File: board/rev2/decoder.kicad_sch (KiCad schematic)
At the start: 2 parts, among them U9 74VHC161

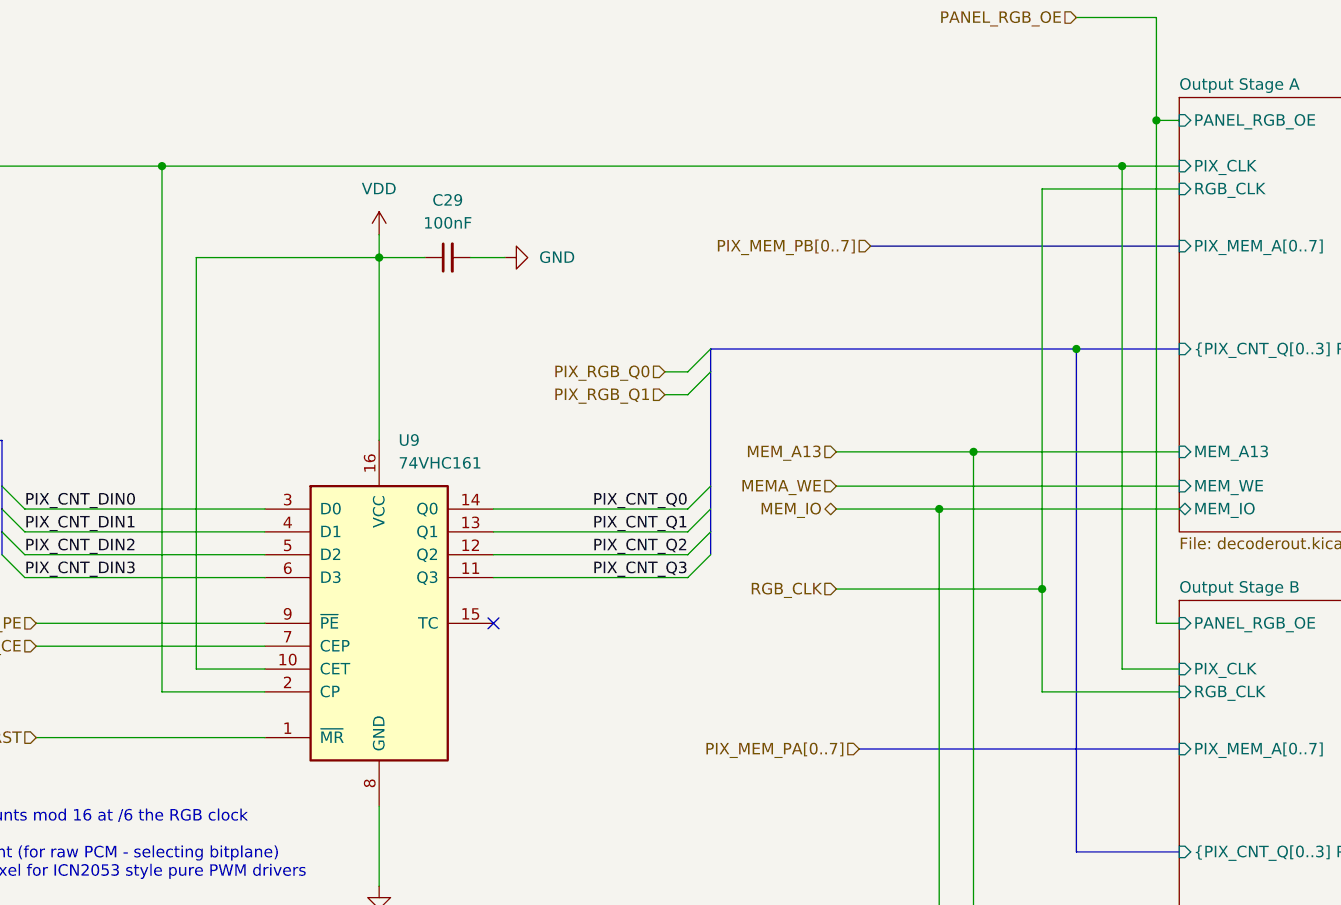
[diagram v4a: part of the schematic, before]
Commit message: Continue board, assign caps/res, adjust for JLC availability
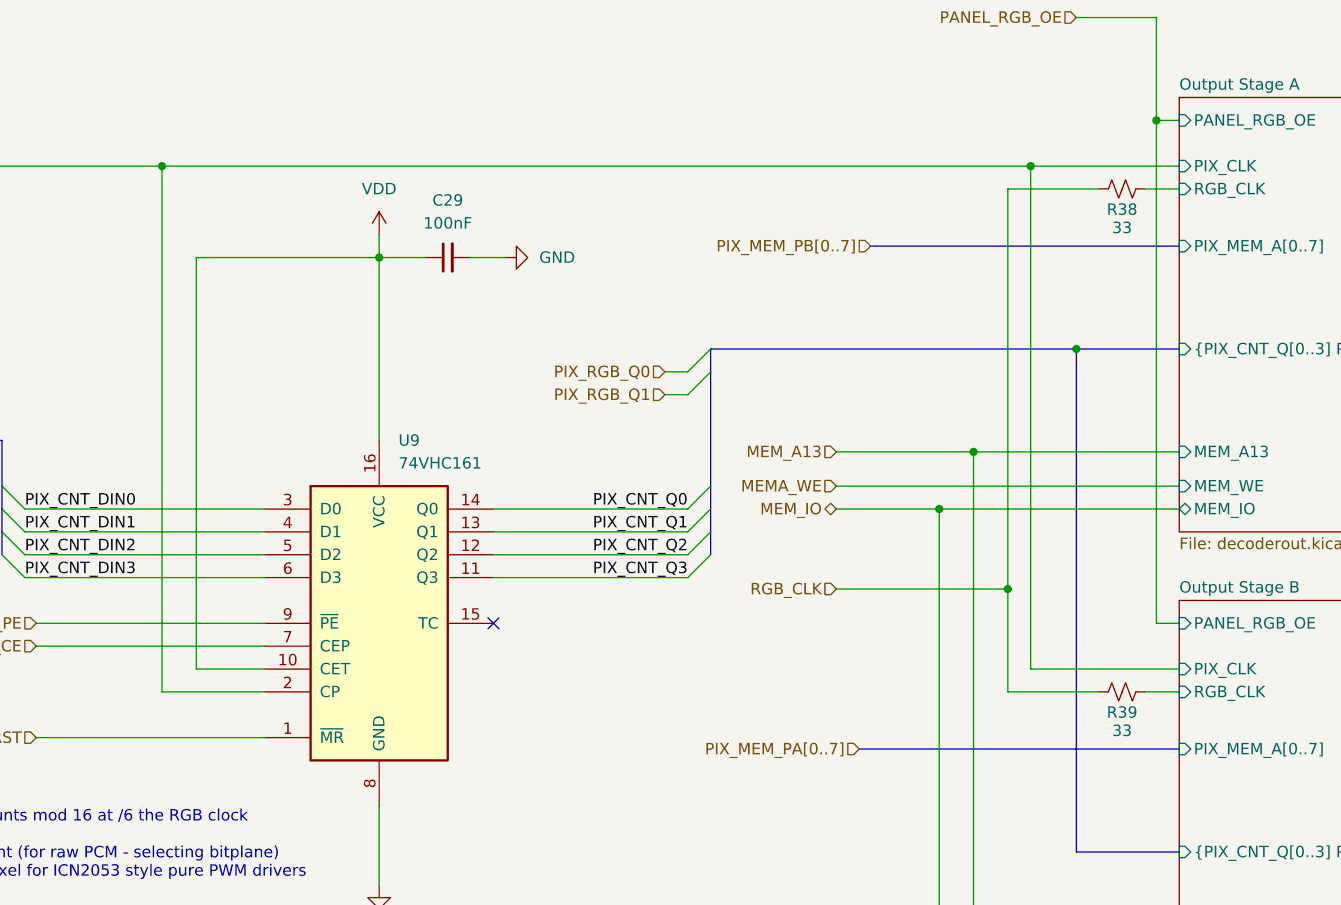
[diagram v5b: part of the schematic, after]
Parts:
- added R38, R39: 33, Resistor_SMD:R_0402_1005Metric, symbol Device:R_Small_US
- C29: footprint (none) -> Capacitor_SMD:C_0402_1005Metric; Part (none) -> CL05B104KB54PNC
- U9: footprint (none) -> Package_SO:TSSOP-16_4.4x5mm_P0.65mm
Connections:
- net RGB_CLK: now also R38.1, R39.1
- new net Output Stage A/RGB_CLK: R38.2
- new net Output Stage B/RGB_CLK: R39.2
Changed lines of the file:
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@@
 	)
 	(junction
-		(at 165.1 95.25)
-		(diameter 0)
-		(color 0 0 0 0)
-	)
-	(junction
-		(at 173.99 48.26)
+		(at 161.29 95.25)
 		(diameter 0)
 		(color 0 0 0 0)
@@
 		(color 0 0 0 0)
 	)
+	(junction
+		(at 163.83 48.26)
+		(diameter 0)
+		(color 0 0 0 0)
+	)
 	(no_connect
 		(at 104.14 99.06)
@@
 	(wire
 		(pts
-			(xy 165.1 95.25) (xy 165.1 50.8)
+			(xy 161.29 95.25) (xy 161.29 50.8)
 		)
 		(stroke
@@
 	(wire
 		(pts
-			(xy 142.24 95.25) (xy 165.1 95.25)
+			(xy 142.24 95.25) (xy 161.29 95.25)
 		)
 		(stroke
@@
 	(wire
 		(pts
-			(xy 165.1 50.8) (xy 180.34 50.8)
-		)
-		(stroke
-			(width 0)
-			(type default)
-		)
-	)
-	(wire
-		(pts
 			(xy 91.44 58.42) (xy 96.52 58.42)
 		)
@@
 	(wire
 		(pts
-			(xy 173.99 48.26) (xy 173.99 104.14)
+			(xy 163.83 48.26) (xy 163.83 104.14)
 		)
 		(stroke
@@
 	(wire
 		(pts
+			(xy 161.29 50.8) (xy 171.45 50.8)
+		)
+		(stroke
+			(width 0)
+			(type default)
+		)
+	)
+	(wire
+		(pts
 			(xy 153.67 86.36) (xy 153.67 142.24)
 		)
@@
 		)
 	)
+	(wire
+		(pts
+			(xy 161.29 106.68) (xy 171.45 106.68)
+		)
+		(stroke
+			(width 0)
+			(type default)
+		)
+	)
 	(bus
 		(pts
@@
 	(wire
 		(pts
-			(xy 165.1 106.68) (xy 180.34 106.68)
-		)
-		(stroke
-			(width 0)
-			(type default)
-		)
-	)
-	(wire
-		(pts
-			(xy 165.1 95.25) (xy 165.1 106.68)
+			(xy 161.29 95.25) (xy 161.29 106.68)
 		)
 		(stroke
@@
 	(wire
 		(pts
-			(xy 67.31 48.26) (xy 173.99 48.26)
+			(xy 176.53 50.8) (xy 180.34 50.8)
+		)
+		(stroke
+			(width 0)
+			(type default)
+		)
+	)
+	(wire
+		(pts
+			(xy 67.31 48.26) (xy 163.83 48.26)
 		)
 		(stroke
@@
 	(wire
 		(pts
+			(xy 176.53 106.68) (xy 180.34 106.68)
+		)
+		(stroke
+			(width 0)
+			(type default)
+		)
+	)
+	(wire
+		(pts
 			(xy 168.91 31.75) (xy 177.8 31.75)
 		)
@@
 		)
 	)
+	(wire
+		(pts
+			(xy 163.83 48.26) (xy 180.34 48.26)
+		)
+		(stroke
+			(width 0)
+			(type default)
+		)
+	)
 	(bus
 		(pts
@@
 	(wire
 		(pts
-			(xy 173.99 48.26) (xy 180.34 48.26)
-		)
-		(stroke
-			(width 0)
-			(type default)
-		)
-	)
-	(wire
-		(pts
 			(xy 142.24 80.01) (xy 157.48 80.01)
 		)
@@
 	(wire
 		(pts
-			(xy 173.99 104.14) (xy 180.34 104.14)
+			(xy 163.83 104.14) (xy 180.34 104.14)
 		)
 		(stroke
@@
 			)
 		)
-		(property "Footprint" ""
+		(property "Footprint" "Package_SO:TSSOP-16_4.4x5mm_P0.65mm"
 			(at 91.44 99.06 0)
 			(effects
@@
 				(path "/32eb05c7-b4a6-42f3-8fb3-43453631100f/2c9586de-ca2f-4a0b-8ff8-8fdad1d1abcc"
 					(reference "U9")
+					(unit 1)
+				)
+			)
+		)
+	)
+	(symbol
+		(lib_id "Device:R_Small_US")
+		(at 173.99 50.8 90)
+		(unit 1)
+		(exclude_from_sim no)
+		(in_bom yes)
+		(on_board yes)
+		(dnp no)
+		(property "Reference" "R38"
+			(at 173.99 53.086 90)
+			(effects
+				(font
+					(size 1.27 1.27)
+				)
+			)
+		)
+		(property "Value" "33"
+			(at 173.99 55.118 90)
+			(effects
+				(font
+					(size 1.27 1.27)
+				)
+			)
+		)
+		(property "Footprint" "Resistor_SMD:R_0402_1005Metric"
+			(at 173.99 50.8 0)
+			(effects
+				(font
+					(size 1.27 1.27)
+				)
+				(hide yes)
+			)
+		)
+		(property "Datasheet" "~"
+			(at 173.99 50.8 0)
+			(effects
+				(font
+					(size 1.27 1.27)
+				)
+				(hide yes)
+			)
+		)
+		(property "Description" "Resistor, small US symbol"
+			(at 173.99 50.8 0)
+			(effects
+				(font
+					(size 1.27 1.27)
+				)
+				(hide yes)
+			)
+		)
+		(property "Part" "0402WGF330JTCE"
+			(at 173.99 50.8 90)
+			(effects
+				(font
+					(size 1.27 1.27)
+				)
+				(hide yes)
+			)
+		)
+		(pin "2"
+		)
+		(pin "1"
+		)
+		(instances
+			(project "mainboard"
+				(path "/32eb05c7-b4a6-42f3-8fb3-43453631100f/2c9586de-ca2f-4a0b-8ff8-8fdad1d1abcc"
+					(reference "R38")
 					(unit 1)
 				)
@@
 			)
 		)
-		(property "Footprint" ""
+		(property "Footprint" "Capacitor_SMD:C_0402_1005Metric"
 			(at 99.06 58.42 0)
 			(effects
@@
 		(property "Description" "Unpolarized capacitor, small symbol"
 			(at 99.06 58.42 0)
+			(effects
+				(font
+					(size 1.27 1.27)
+				)
+				(hide yes)
+			)
+		)
+		(property "Part" "CL05B104KB54PNC"
+			(at 99.06 58.42 90)
 			(effects
 				(font
@@
 					(unit 1)
 				)
+			)
+		)
+	)
+	(symbol
+		(lib_id "Device:R_Small_US")
+		(at 173.99 106.68 90)
+		(unit 1)
+		(exclude_from_sim no)
+		(in_bom yes)
+		(on_board yes)
+		(dnp no)
+		(property "Reference" "R39"
+			(at 173.99 108.966 90)
+			(effects
+				(font
+					(size 1.27 1.27)
+				)
+			)
+		)
+		(property "Value" "33"
+			(at 173.99 110.998 90)
+			(effects
+				(font
+					(size 1.27 1.27)
+				)
+			)
+		)
+		(property "Footprint" "Resistor_SMD:R_0402_1005Metric"
+			(at 173.99 106.68 0)
+			(effects
+				(font
+					(size 1.27 1.27)
+				)
+				(hide yes)
+			)
+		)
+		(property "Datasheet" "~"
+			(at 173.99 106.68 0)
+			(effects
+				(font
+					(size 1.27 1.27)
+				)
+				(hide yes)
+			)
+		)
+		(property "Description" "Resistor, small US symbol"
+			(at 173.99 106.68 0)
+			(effects
+				(font
+					(size 1.27 1.27)
+				)
+				(hide yes)
+			)
+		)
+		(property "Part" "0402WGF330JTCE"
+			(at 173.99 106.68 90)
+			(effects
+				(font
+					(size 1.27 1.27)
+				)
+				(hide yes)
+			)
+		)
+		(pin "2"
+		)
+		(pin "1"
+		)
+		(instances
+			(project ""
+				(path "/32eb05c7-b4a6-42f3-8fb3-43453631100f/2c9586de-ca2f-4a0b-8ff8-8fdad1d1abcc"
+					(reference "R39")
+					(unit 1)
+				)

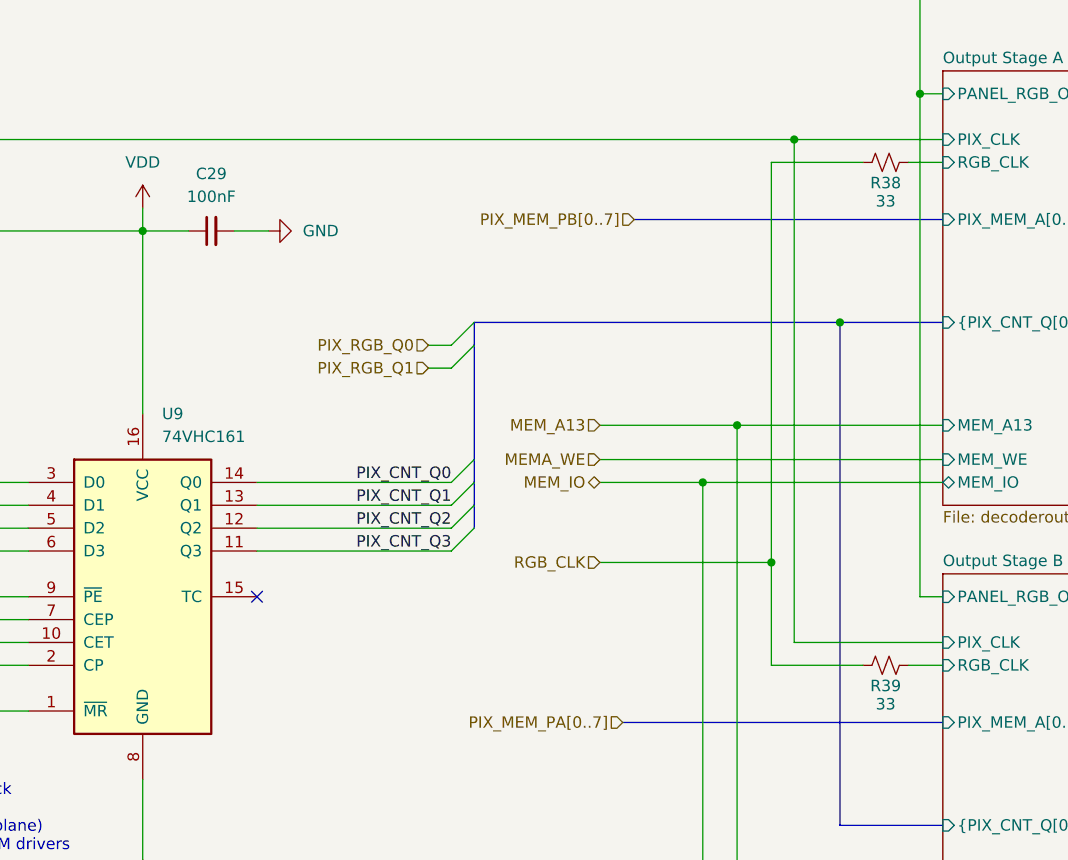
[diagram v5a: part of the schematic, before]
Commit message: Start new PCB
- all footprints setup
- need to setup netclasses next, tho
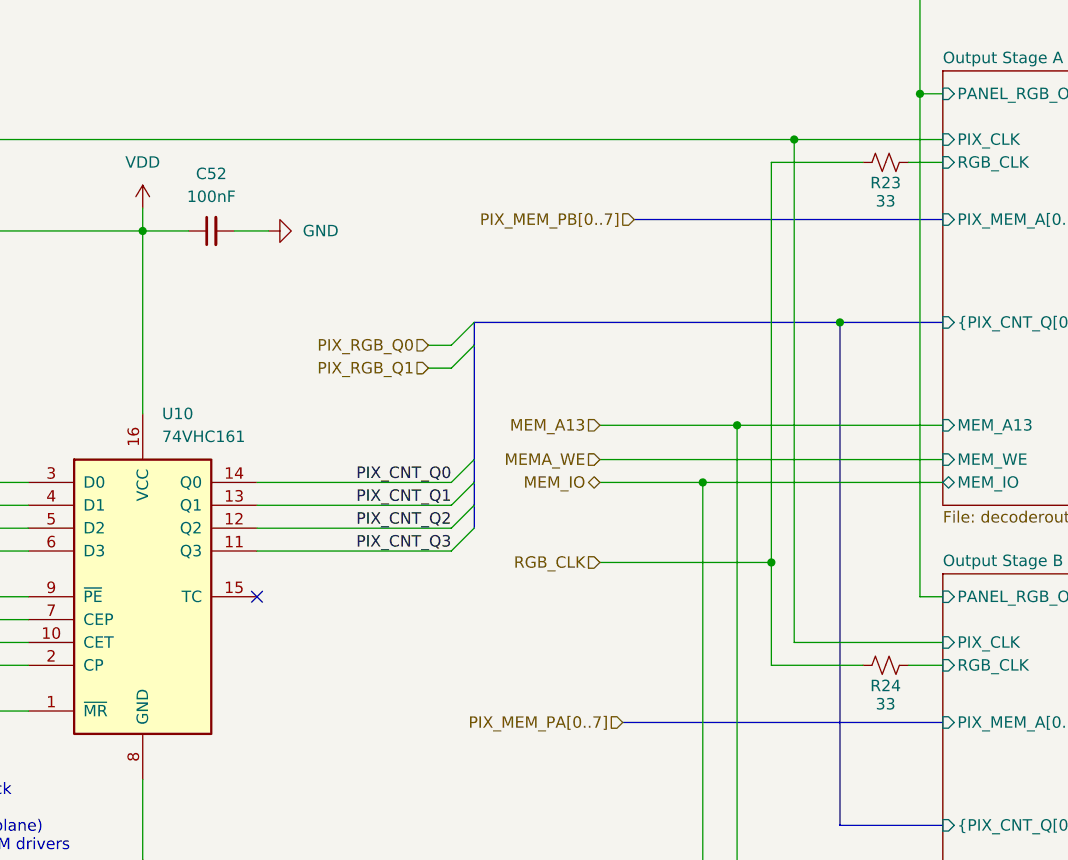
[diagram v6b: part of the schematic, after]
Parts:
- U10: renamed from U9; Part (none) -> 74VHC161
- renumbered C29 to C52, R38 to R23, R39 to R24
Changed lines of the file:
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@@
 		(dnp no)
 		(fields_autoplaced yes)
-		(property "Reference" "U9"
+		(property "Reference" "U10"
 			(at 93.5833 78.74 0)
 			(effects
@@
 			)
 		)
+		(property "Part" "74VHC161"
+			(at 91.44 99.06 0)
+			(effects
+				(font
+					(size 1.27 1.27)
+				)
+				(hide yes)
+			)
+		)
 		(pin "7"
 		)
@@
 			(project "mainboard"
 				(path "/32eb05c7-b4a6-42f3-8fb3-43453631100f/2c9586de-ca2f-4a0b-8ff8-8fdad1d1abcc"
-					(reference "U9")
+					(reference "U10")
 					(unit 1)
 				)
@@
 		(on_board yes)
 		(dnp no)
-		(property "Reference" "R38"
+		(property "Reference" "R23"
 			(at 173.99 53.086 90)
 			(effects
@@
 			(project "mainboard"
 				(path "/32eb05c7-b4a6-42f3-8fb3-43453631100f/2c9586de-ca2f-4a0b-8ff8-8fdad1d1abcc"
-					(reference "R38")
+					(reference "R23")
 					(unit 1)
 				)
@@
 		(dnp no)
 		(fields_autoplaced yes)
-		(property "Reference" "C29"
+		(property "Reference" "C52"
 			(at 99.0663 52.07 90)
 			(effects
@@
 			(project ""
 				(path "/32eb05c7-b4a6-42f3-8fb3-43453631100f/2c9586de-ca2f-4a0b-8ff8-8fdad1d1abcc"
-					(reference "C29")
+					(reference "C52")
 					(unit 1)
 				)
@@
 		(dnp no)
 		(fields_autoplaced yes)
-		(property "Reference" "#PWR030"
+		(property "Reference" "#PWR034"
 			(at 111.76 58.42 0)
 			(effects
@@
 			(project ""
 				(path "/32eb05c7-b4a6-42f3-8fb3-43453631100f/2c9586de-ca2f-4a0b-8ff8-8fdad1d1abcc"
-					(reference "#PWR030")
+					(reference "#PWR034")
 					(unit 1)
 				)
@@
 		(on_board yes)
 		(dnp no)
-		(property "Reference" "R39"
+		(property "Reference" "R24"
 			(at 173.99 108.966 90)
 			(effects
@@
 			(project ""
 				(path "/32eb05c7-b4a6-42f3-8fb3-43453631100f/2c9586de-ca2f-4a0b-8ff8-8fdad1d1abcc"
-					(reference "R39")
+					(reference "R24")
 					(unit 1)
 				)
@@
 		(dnp no)
 		(fields_autoplaced yes)
-		(property "Reference" "#PWR24"
+		(property "Reference" "#PWR033"
 			(at 91.44 134.62 0)
 			(effects
@@
 			(project "mainboard"
 				(path "/32eb05c7-b4a6-42f3-8fb3-43453631100f/2c9586de-ca2f-4a0b-8ff8-8fdad1d1abcc"
-					(reference "#PWR24")
+					(reference "#PWR033")
 					(unit 1)
 				)
@@
 		(dnp no)
 		(fields_autoplaced yes)
-		(property "Reference" "#PWR20"
+		(property "Reference" "#PWR032"
 			(at 91.44 59.69 0)
 			(effects
@@
 			(project "mainboard"
 				(path "/32eb05c7-b4a6-42f3-8fb3-43453631100f/2c9586de-ca2f-4a0b-8ff8-8fdad1d1abcc"
-					(reference "#PWR20")
-					(unit 1)
-				)
+					(reference "#PWR032")
+					(unit 1)
+				)
